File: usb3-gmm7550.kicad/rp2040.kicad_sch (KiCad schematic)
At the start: 58 parts, among them J2 USB_C_Receptacle_USB2.0, J3 SWD, SW4 SW_Push, SW5 SW_Push, SW6 SW_DIP_x02, U12 AP7330, U13 AP7330, U14 MX25R1635FZU, U15 ECMF02-2AMX6, U16 LM4040DBZ-3, U17 RP2040, Y1 445I23D12M00000

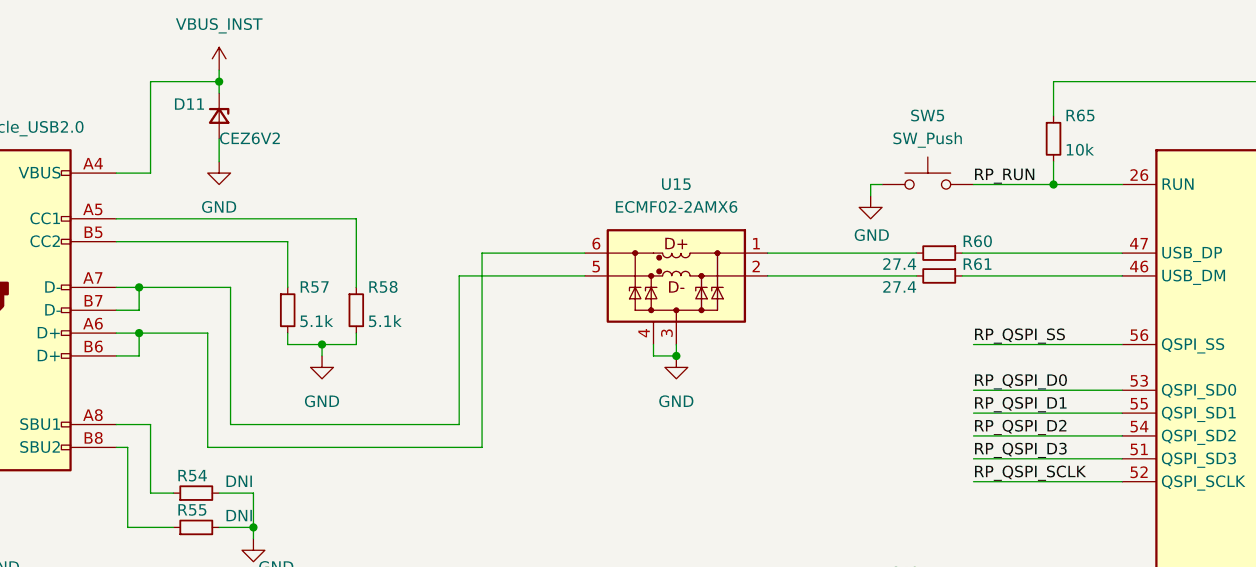
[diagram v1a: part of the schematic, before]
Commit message: Connect USB 3 SuperSpeed diff. pairs
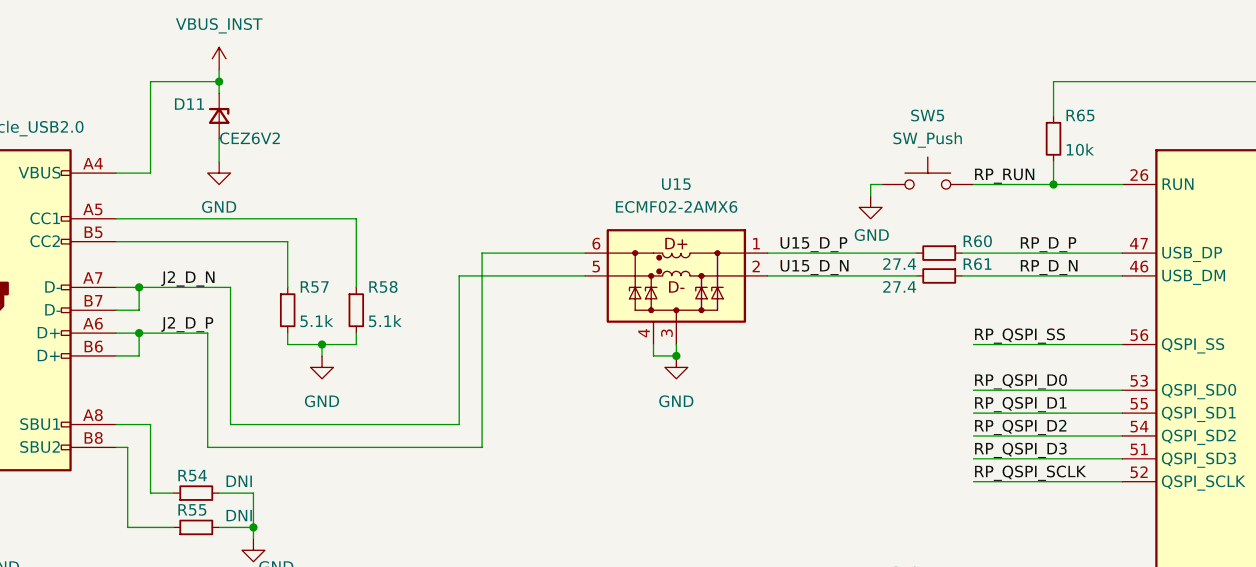
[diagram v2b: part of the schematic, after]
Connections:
- net U15_D_P: now reaches R60.2, U15.1 (D+_in)
- net U15_D_N: now reaches R61.2, U15.2 (D-_in)
- net J2_D_N: now reaches J2.A7 (D-), J2.B7 (D-), U15.5 (D-_out)
- net J2_D_P: now reaches J2.A6 (D+), J2.B6 (D+), U15.6 (D+_out)
- net RP_D_P: now reaches R60.1, U17.47 (USB_DP)
- net RP_D_N: now reaches R61.1, U17.46 (USB_DM)
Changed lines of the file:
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@@
+		)
+	)
+	(label "J2_D_N"
+		(at 50.8 49.53 0)
+		(effects
+			(font
+				(size 1.27 1.27)
+			)
+			(justify left bottom)
 		)
 	)
@@
 		)
 	)
+	(label "RP_D_N"
+		(at 146.05 48.26 0)
+		(effects
+			(font
+				(size 1.27 1.27)
+			)
+			(justify left bottom)
+		)
+	)
 	(label "RP_QSPI_D1"
 		(at 140.97 63.5 0)
@@
 		)
 	)
+	(label "RP_D_P"
+		(at 146.05 45.72 0)
+		(effects
+			(font
+				(size 1.27 1.27)
+			)
+			(justify left bottom)
+		)
+	)
 	(label "RP_QSPI_SS"
 		(at 58.42 100.33 0)
+		(effects
+			(font
+				(size 1.27 1.27)
+			)
+			(justify left bottom)
+		)
+	)
+	(label "U15_D_N"
+		(at 119.38 48.26 0)
 		(effects
 			(font
@@
 		(effects
 			(font
+				(size 1.27 1.27)
+			)
+			(justify left bottom)
+		)
+	)
+	(label "J2_D_P"
+		(at 50.8 54.61 0)
+		(effects
+			(font
+				(size 1.27 1.27)
+			)
+			(justify left bottom)
+		)
+	)
+	(label "U15_D_P"
+		(at 119.38 45.72 0)
+		(effects
+			(font

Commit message: Layout WIP: split power plane (internal layer 2)
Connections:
- net IO_SB_A7 renamed IO_SB_A5
- net IO_SB_B7 renamed IO_SB_A1
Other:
- note added: "CLK_IN0"
- note added: "CLK_OUT1 (GateMate CLK3)"
- note added: "CLK_OUT2"
- note added: "CLK_OUT3"
- note added: "I2C1 (GPIO Function 3)"
- note added: "SPI1 (GPIO Function 1)"
- note added: "UART0 (GPIO Function 2)"
- note removed: "CLK0"
- note removed: "CLK1"
- note removed: "CLK2"
- note removed: "CLK3"
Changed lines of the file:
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@@
 		(rev "0.9.5")
 	)
-	(text "CLK0"
+	(text "CLK_IN0"
 		(exclude_from_sim no)
-		(at 238.76 92.71 0)
+		(at 238.76 89.535 0)
 		(effects
 			(font
@@
 		)
 	)
-	(text "CLK1"
+	(text "CLK_OUT1 (GateMate CLK3)"
 		(exclude_from_sim no)
 		(at 238.76 97.79 0)
@@
 		)
 	)
+	(text "I2C1 (GPIO Function 3)"
+		(exclude_from_sim no)
+		(at 238.76 44.45 0)
+		(effects
+			(font
+				(size 1.27 1.27)
+			)
+			(justify left)
+		)
+	)
 	(text "Vout=2.5V"
 		(exclude_from_sim no)
@@
 		)
 	)
-	(text "CLK3"
+	(text "CLK_OUT3"
 		(exclude_from_sim no)
 		(at 238.76 102.87 0)
@@
 		)
 	)
+	(text "UART0 (GPIO Function 2)"
+		(exclude_from_sim no)
+		(at 238.76 69.85 0)
+		(effects
+			(font
+				(size 1.27 1.27)
+			)
+			(justify left)
+		)
+	)
 	(text "1-4 Enable Module Power\n2-3 Disable RP2040"
 		(exclude_from_sim no)
@@
 		)
 	)
-	(text "CLK2"
+	(text "CLK_OUT2"
 		(exclude_from_sim no)
 		(at 238.76 100.33 0)
@@
 		)
 	)
+	(text "SPI1 (GPIO Function 1)"
+		(exclude_from_sim no)
+		(at 238.76 62.23 0)
+		(effects
+			(font
+				(size 1.27 1.27)
+			)
+			(justify left)
+		)
+	)
 	(text_box "NOTE: IO pin assignment may be changed to facilitate layout"
 		(exclude_from_sim no)
@@
 		)
 	)
+	(polyline
+		(pts
+			(xy 236.22 66.04) (xy 237.49 66.04)
+		)
+		(stroke
+			(width 0)
+			(type default)
+		)
+	)
 	(wire
 		(pts
@@
 		)
 	)
+	(polyline
+		(pts
+			(xy 236.22 58.42) (xy 237.49 58.42)
+		)
+		(stroke
+			(width 0)
+			(type default)
+		)
+	)
 	(wire
 		(pts
@@
 		)
 	)
+	(polyline
+		(pts
+			(xy 236.22 43.18) (xy 237.49 43.18)
+		)
+		(stroke
+			(width 0)
+			(type default)
+		)
+	)
 	(wire
 		(pts
@@
 		)
 	)
+	(polyline
+		(pts
+			(xy 237.49 58.42) (xy 237.49 66.04)
+		)
+		(stroke
+			(width 0)
+			(type default)
+		)
+	)
 	(wire
 		(pts
@@
 		)
 	)
+	(polyline
+		(pts
+			(xy 236.22 45.72) (xy 237.49 45.72)
+		)
+		(stroke
+			(width 0)
+			(type default)
+		)
+	)
 	(wire
 		(pts
@@
 		)
 	)
+	(polyline
+		(pts
+			(xy 236.22 68.58) (xy 237.49 68.58)
+		)
+		(stroke
+			(width 0)
+			(type default)
+		)
+	)
 	(wire
 		(pts
@@
 		)
 	)
+	(polyline
+		(pts
+			(xy 237.49 43.18) (xy 237.49 45.72)
+		)
+		(stroke
+			(width 0)
+			(type default)
+		)
+	)
 	(wire
 		(pts
@@
 		)
 	)
+	(polyline
+		(pts
+			(xy 237.49 68.58) (xy 237.49 71.12)
+		)
+		(stroke
+			(width 0)
+			(type default)
+		)
+	)
 	(wire
 		(pts
@@
 		)
 	)
+	(polyline
+		(pts
+			(xy 236.22 71.12) (xy 237.49 71.12)
+		)
+		(stroke
+			(width 0)
+			(type default)
+		)
+	)
 	(wire
 		(pts
@@
 		)
 	)
+	(global_label "IO_SB_A1"
+		(shape bidirectional)
+		(at 223.52 99.06 0)
+		(fields_autoplaced yes)
+		(effects
+			(font
+				(size 1.27 1.27)
+			)
+			(justify left)
+		)
+		(property "Intersheetrefs" "${INTERSHEET_REFS}"
+			(at 236.2646 99.06 0)
+			(effects
+				(font
+					(size 1.27 1.27)
+				)
+				(justify left)
+				(hide yes)
+			)
+		)
+	)
 	(global_label "TDI"
 		(shape input)
@@
 		)
 	)
-	(global_label "IO_SB_A7"
+	(global_label "IO_SB_A5"
 		(shape bidirectional)
 		(at 223.52 96.52 0)
@@
 			(effects
 				(font
-					(size 1.27 1.27)
-				)
-				(justify left)
-				(hide yes)
-			)
-		)
-	)
-	(global_label "IO_SB_B7"
-		(shape bidirectional)
-		(at 223.52 99.06 0)
-		(fields_autoplaced yes)
-		(effects
-			(font
-				(size 1.27 1.27)
-			)
-			(justify left)
-		)
-		(property "Intersheetrefs" "${INTERSHEET_REFS}"
-			(at 236.446 99.06 0)
-			(effects
-				(font

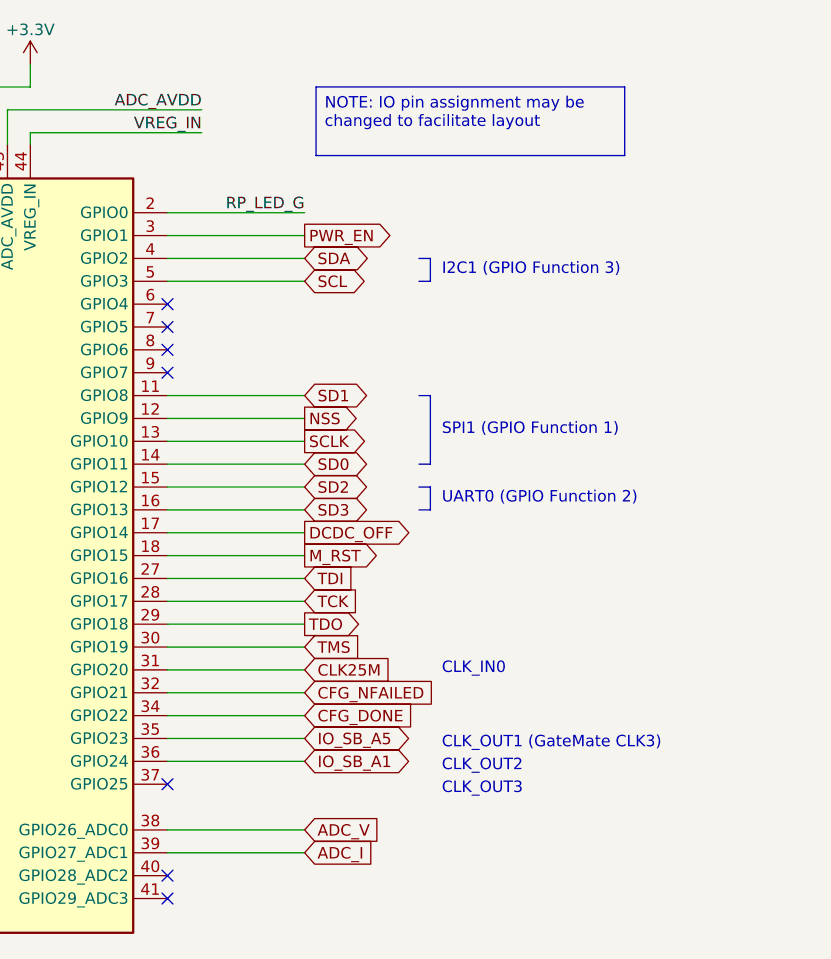
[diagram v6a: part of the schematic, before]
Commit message: Layout [almost] complete -- all connections are routed
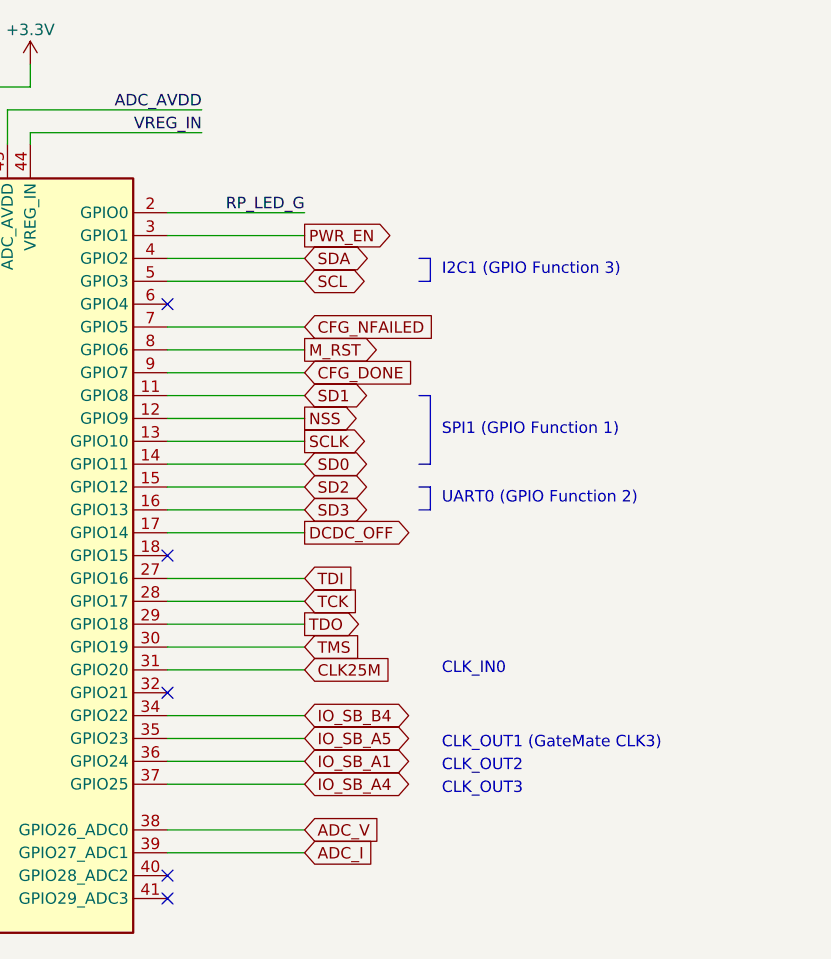
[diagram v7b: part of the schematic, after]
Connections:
- net CFG_DONE: now also U17.9 (GPIO7); no longer U17.34 (GPIO22)
- net CFG_NFAILED: now also U17.7 (GPIO5); no longer U17.32 (GPIO21)
- net M_RST: now also U17.8 (GPIO6); no longer U17.18 (GPIO15)
- net IO_SB_A4: now reaches U17.37 (GPIO25)
- new net IO_SB_B4: U17.34 (GPIO22)
- no-connect marks 7 -> 5
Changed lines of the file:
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@@
 		)
 	)
-	(text_box "NOTE: IO pin assignment may be changed to facilitate layout"
-		(exclude_from_sim no)
-		(at 224.79 24.13 0)
-		(size 34.29 7.62)
-		(margins 0.9525 0.9525 0.9525 0.9525)
-		(stroke
-			(width 0)
-			(type solid)
-		)
-		(fill
-			(type color)
-			(color 255 234 69 1)
-		)
-		(effects
-			(font
-				(size 1.27 1.27)
-			)
-			(justify left top)
-		)
-	)
 	(junction
 		(at 182.88 123.19)
@@
 	)
 	(no_connect
-		(at 208.28 55.88)
-	)
-	(no_connect
-		(at 208.28 101.6)
+		(at 208.28 91.44)
 	)
 	(no_connect
@@
 	)
 	(no_connect
-		(at 208.28 53.34)
-	)
-	(no_connect
-		(at 208.28 50.8)
+		(at 208.28 76.2)
 	)
 	(no_connect
@@
 	(wire
 		(pts
-			(xy 208.28 93.98) (xy 223.52 93.98)
-		)
-		(stroke
-			(width 0)
-			(type default)
-		)
-	)
-	(wire
-		(pts
 			(xy 45.72 52.07) (xy 48.26 52.07)
 		)
@@
 	(wire
 		(pts
+			(xy 208.28 53.34) (xy 223.52 53.34)
+		)
+		(stroke
+			(width 0)
+			(type default)
+		)
+	)
+	(wire
+		(pts
 			(xy 190.5 26.67) (xy 212.09 26.67)
 		)
@@
 	(wire
 		(pts
+			(xy 208.28 55.88) (xy 223.52 55.88)
+		)
+		(stroke
+			(width 0)
+			(type default)
+		)
+	)
+	(wire
+		(pts
 			(xy 255.27 128.27) (xy 257.81 128.27)
 		)
@@
 	(wire
 		(pts
-			(xy 208.28 76.2) (xy 223.52 76.2)
-		)
-		(stroke
-			(width 0)
-			(type default)
-		)
-	)
-	(wire
-		(pts
 			(xy 127 83.82) (xy 127 93.98)
 		)
@@
 	(wire
 		(pts
+			(xy 208.28 93.98) (xy 223.52 93.98)
+		)
+		(stroke
+			(width 0)
+			(type default)
+		)
+	)
+	(wire
+		(pts
 			(xy 71.12 154.94) (xy 71.12 156.21)
 		)
@@
 	(wire
 		(pts
+			(xy 208.28 101.6) (xy 223.52 101.6)
+		)
+		(stroke
+			(width 0)
+			(type default)
+		)
+	)
+	(wire
+		(pts
 			(xy 96.52 97.79) (xy 96.52 100.33)
 		)
@@
 	(wire
 		(pts
+			(xy 208.28 50.8) (xy 223.52 50.8)
+		)
+		(stroke
+			(width 0)
+			(type default)
+		)
+	)
+	(wire
+		(pts
 			(xy 58.42 49.53) (xy 58.42 64.77)
 		)
@@
 	(wire
 		(pts
-			(xy 208.28 91.44) (xy 223.52 91.44)
-		)
-		(stroke
-			(width 0)
-			(type default)
-		)
-	)
-	(wire
-		(pts
 			(xy 100.33 146.05) (xy 115.57 146.05)
 		)
@@
 	(global_label "M_RST"
 		(shape output)
-		(at 223.52 76.2 0)
+		(at 223.52 53.34 0)
 		(fields_autoplaced yes)
 		(effects
@@
 		)
 		(property "Intersheetrefs" "${INTERSHEET_REFS}"
-			(at 231.7171 76.2 0)
+			(at 231.7171 53.34 0)
 			(effects
 				(font
@@
 		)
 	)
+	(global_label "IO_SB_A4"
+		(shape bidirectional)
+		(at 223.52 101.6 0)
+		(fields_autoplaced yes)
+		(effects
+			(font
+				(size 1.27 1.27)
+			)
+			(justify left)
+		)
+		(property "Intersheetrefs" "${INTERSHEET_REFS}"
+			(at 236.2646 101.6 0)
+			(effects
+				(font
+					(size 1.27 1.27)
+				)
+				(justify left)
+				(hide yes)
+			)
+		)
+	)
 	(global_label "SDA"
 		(shape bidirectional)
@@
 		)
 	)
+	(global_label "IO_SB_B4"
+		(shape bidirectional)
+		(at 223.52 93.98 0)
+		(fields_autoplaced yes)
+		(effects
+			(font
+				(size 1.27 1.27)
+			)
+			(justify left)
+		)
+		(property "Intersheetrefs" "${INTERSHEET_REFS}"
+			(at 236.446 93.98 0)
+			(effects
+				(font
+					(size 1.27 1.27)
+				)
+				(justify left)
+				(hide yes)
+			)
+		)
+	)
 	(global_label "SD2"
 		(shape bidirectional)
@@
 	(global_label "CFG_DONE"
 		(shape input)
-		(at 223.52 93.98 0)
+		(at 223.52 55.88 0)
 		(fields_autoplaced yes)
 		(effects
@@
 		)
 		(property "Intersheetrefs" "${INTERSHEET_REFS}"
-			(at 235.5272 93.98 0)
+			(at 235.5272 55.88 0)
 			(effects
 				(font
@@
 	(global_label "CFG_NFAILED"
 		(shape input)
-		(at 223.52 91.44 0)
+		(at 223.52 50.8 0)
 		(fields_autoplaced yes)
 		(effects
@@
 		)
 		(property "Intersheetrefs" "${INTERSHEET_REFS}"
-			(at 238.0068 91.44 0)
+			(at 238.0068 50.8 0)
 			(effects
 				(font

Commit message: Final touches -- revision 1.0 schematic is released
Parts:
- U12, U13: value AP7330 -> AP7330D
- U14: value MX25R1635FZU -> MX25R1635FZUIH0
- U16: value LM4040DBZ-3 -> LM4040A30IDBZ
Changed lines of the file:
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@@
 	(title_block
 		(title "GMM-7550 USB3 Adapter")
-		(date "2025-10-01")
-		(rev "0.9.5")
+		(date "2025-10-10")
+		(rev "1.0")
 	)
 	(text "CLK_IN0"
@@
 			)
 		)
-		(property "Value" "MX25R1635FZU"
+		(property "Value" "MX25R1635FZUIH0"
 			(at 88.9 121.92 0)
 			(effects
@@
 			)
 		)
-		(property "Value" "AP7330"
+		(property "Value" "AP7330D"
 			(at 58.42 171.45 0)
 			(effects
@@
 			)
 		)
-		(property "Value" "LM4040DBZ-3"
+		(property "Value" "LM4040A30IDBZ"
 			(at 130.175 152.4 90)
 			(effects
@@
 			)
 		)
-		(property "Value" "AP7330"
+		(property "Value" "AP7330D"
 			(at 58.42 144.78 0)
 			(effects
